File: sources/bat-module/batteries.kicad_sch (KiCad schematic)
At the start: 15 parts, among them J1 53261-0871, J3 67996-110HLF

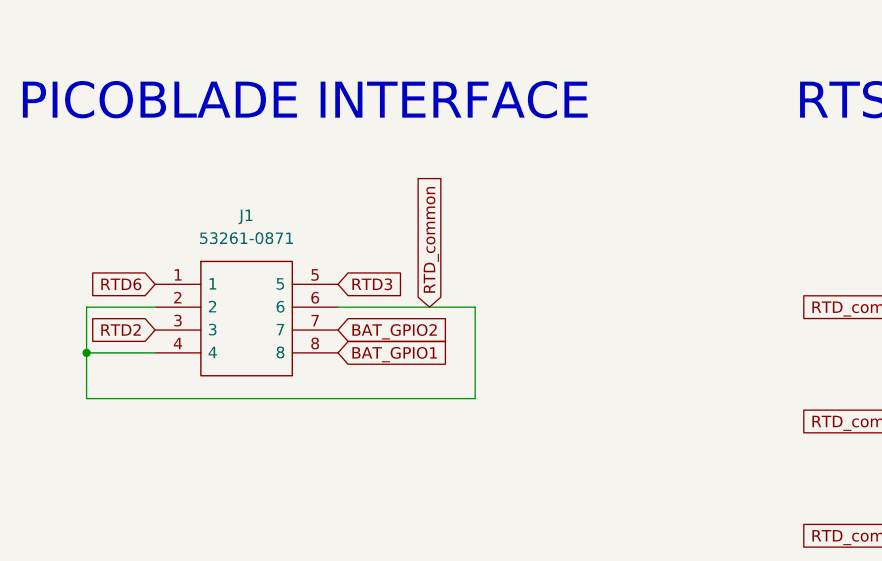
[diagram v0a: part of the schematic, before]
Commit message: i2c-obdh connection and removing picoblade interface #3 #4
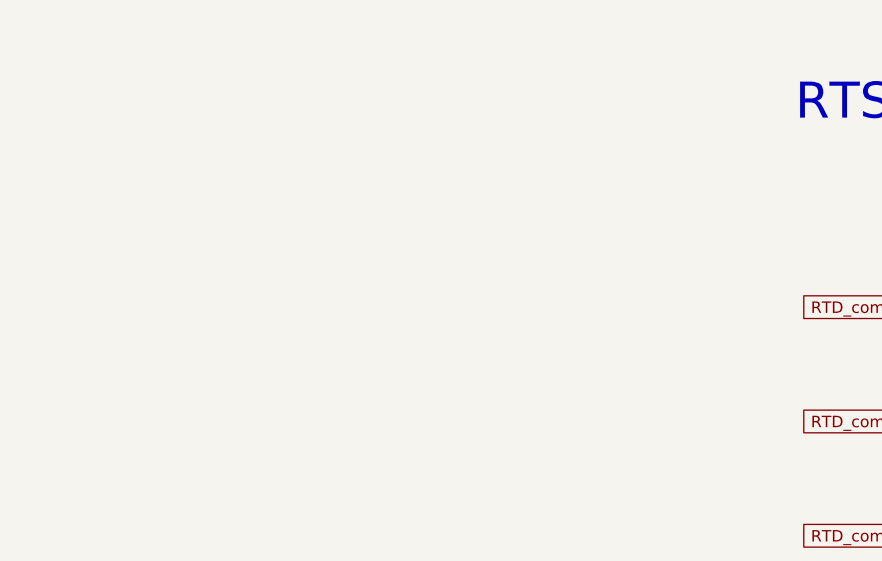
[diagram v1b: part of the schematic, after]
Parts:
- removed J1: 53261-0871, symbol 53261-0871:53261-0871
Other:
- note removed: "PICOBLADE INTERFACE"
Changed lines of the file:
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@@
   (junction (at 241.3 55.88) (diameter 0) (color 0 0 0 0)
   )
-  (junction (at 38.1 68.58) (diameter 0) (color 0 0 0 0)
-  )
   (junction (at 78.74 152.4) (diameter 0) (color 0 0 0 0)
   )
@@
     (stroke (width 0) (type default))
   )
-  (wire (pts (xy 38.1 68.58) (xy 38.1 63.5))
-    (stroke (width 0) (type default))
-  )
   (wire (pts (xy 53.34 160.02) (xy 58.42 160.02))
     (stroke (width 0) (type default))
@@
     (stroke (width 0) (type default))
   )
-  (wire (pts (xy 81.28 63.5) (xy 81.28 73.66))
-    (stroke (width 0) (type default))
-  )
   (wire (pts (xy 210.82 55.88) (xy 215.9 55.88))
     (stroke (width 0) (type default))
@@
     (stroke (width 0) (type default))
   )
-  (wire (pts (xy 81.28 73.66) (xy 38.1 73.66))
-    (stroke (width 0) (type default))
-  )
   (wire (pts (xy 208.28 139.7) (xy 213.36 139.7))
     (stroke (width 0) (type default))
@@
     (stroke (width 0) (type default))
   )
-  (wire (pts (xy 66.04 63.5) (xy 81.28 63.5))
-    (stroke (width 0) (type default))
-  )
   (wire (pts (xy 215.9 76.2) (xy 220.98 76.2))
     (stroke (width 0) (type default))
@@
     (stroke (width 0) (type default))
   )
-  (wire (pts (xy 38.1 63.5) (xy 45.72 63.5))
-    (stroke (width 0) (type default))
-  )
   (wire (pts (xy 45.72 134.62) (xy 58.42 134.62))
     (stroke (width 0) (type default))
@@
     (stroke (width 0) (type default))
   )
-  (wire (pts (xy 45.72 68.58) (xy 38.1 68.58))
-    (stroke (width 0) (type default))
-  )
   (wire (pts (xy 241.3 144.78) (xy 241.3 142.24))
     (stroke (width 0) (type default))
@@
     (stroke (width 0) (type default))
   )
-  (wire (pts (xy 38.1 68.58) (xy 38.1 73.66))
-    (stroke (width 0) (type default))
-  )
   (wire (pts (xy 208.28 147.32) (xy 213.36 147.32))
     (stroke (width 0) (type default))
-  )
-  (text "PICOBLADE INTERFACE" (at 30.48 43.18 0)
-    (effects (font (face "KiCad Font") (size 4 4)) (justify left bottom))
   )
   (text "BATTERIES BOARD TO BOARD \nCONNECTOR TO EPS\n" (at 187.96 124.46 0)
@@
     (effects (font (face "KiCad Font") (size 4 4)) (justify left bottom))
   )
-  (global_label "RTD3" (shape input) (at 66.04 60.96 0) (fields_autoplaced)
-    (effects (font (size 1.27 1.27)) (justify left))
-    (property "Intersheetrefs" "${INTERSHEET_REFS}" (at 73.7423 60.96 0)
-      (effects (font (size 1.27 1.27)) (justify left) hide)
-    )
-  )
   (global_label "VBus" (shape input) (at 243.84 76.2 0) (fields_autoplaced)
     (effects (font (size 1.27 1.27)) (justify left))
@@
     )
   )
-  (global_label "RTD_common" (shape input) (at 76.2 63.5 90) (fields_autoplaced)
-    (effects (font (size 1.27 1.27)) (justify left))
-    (property "Intersheetrefs" "${INTERSHEET_REFS}" (at 76.2 48.1174 90)
-      (effects (font (size 1.27 1.27)) (justify left) hide)
-    )
-  )
   (global_label "-Heater1_Voltage" (shape input) (at 210.82 50.8 180) (fields_autoplaced)
     (effects (font (size 1.27 1.27)) (justify right))
@@
     )
   )
-  (global_label "BAT_GPIO2" (shape input) (at 66.04 66.04 0) (fields_autoplaced)
-    (effects (font (size 1.27 1.27)) (justify left))
-    (property "Intersheetrefs" "${INTERSHEET_REFS}" (at 79.0038 66.04 0)
-      (effects (font (size 1.27 1.27)) (justify left) hide)
-    )
-  )
   (global_label "-VBat" (shape input) (at 53.34 147.32 180) (fields_autoplaced)
     (effects (font (size 1.27 1.27)) (justify right))
@@
     )
   )
-  (global_label "RTD2" (shape input) (at 45.72 66.04 180) (fields_autoplaced)
-    (effects (font (size 1.27 1.27)) (justify right))
-    (property "Intersheetrefs" "${INTERSHEET_REFS}" (at 38.0177 66.04 0)
-      (effects (font (size 1.27 1.27)) (justify right) hide)
-    )
-  )
   (global_label "-VBat" (shape input) (at 203.2 142.24 180) (fields_autoplaced)
     (effects (font (size 1.27 1.27)) (justify right))
@@
     )
   )
-  (global_label "BAT_GPIO1" (shape input) (at 66.04 68.58 0) (fields_autoplaced)
-    (effects (font (size 1.27 1.27)) (justify left))
-    (property "Intersheetrefs" "${INTERSHEET_REFS}" (at 79.0038 68.58 0)
-      (effects (font (size 1.27 1.27)) (justify left) hide)
-    )
-  )
   (global_label "RTD_common" (shape input) (at 132.08 88.9 180) (fields_autoplaced)
     (effects (font (size 1.27 1.27)) (justify right))
@@
     (property "Intersheetrefs" "${INTERSHEET_REFS}" (at 266.2984 50.8 0)
       (effects (font (size 1.27 1.27)) (justify left) hide)
-    )
-  )
-  (global_label "RTD6" (shape input) (at 45.72 60.96 180) (fields_autoplaced)
-    (effects (font (size 1.27 1.27)) (justify right))
-    (property "Intersheetrefs" "${INTERSHEET_REFS}" (at 38.0177 60.96 0)
-      (effects (font (size 1.27 1.27)) (justify right) hide)
     )
   )
@@
         )
       )
-    )
-  )
-  (symbol (lib_id "53261-0871:53261-0871") (at 45.72 60.96 0) (unit 1)
-    (in_bom yes) (on_board yes) (dnp no) (fields_autoplaced)
-    (property "Reference" "J1" (at 55.88 53.34 0)
-      (effects (font (size 1.27 1.27)))
-    )
-    (property "Value" "53261-0871" (at 55.88 55.88 0)
-      (effects (font (size 1.27 1.27)))
-    )
-    (property "Footprint" "" (at 62.23 58.42 0)
-      (effects (font (size 1.27 1.27)) (justify left) hide)
-    )
-    (property "Datasheet" "http://www.molex.com/webdocs/datasheets/pdf/en-us/0532610871_PCB_HEADERS.pdf" (at 62.23 60.96 0)
-      (effects (font (size 1.27 1.27)) (justify left) hide)
-    )
-    (property "Description" "Molex PICOBLADE Series, Series Number 53261, 1.25mm Pitch, 8 Way 1 Row Shrouded Right Angle PCB Header, Surface Mount" (at 62.23 63.5 0)
-      (effects (font (size 1.27 1.27)) (justify left) hide)
-    )
-    (property "Height" "" (at 62.23 66.04 0)
-      (effects (font (size 1.27 1.27)) (justify left) hide)
-    )
-    (property "Mouser Part Number" "538-53261-0871" (at 62.23 68.58 0)
-      (effects (font (size 1.27 1.27)) (justify left) hide)
-    )
-    (property "Mouser Price/Stock" "https://www.mouser.co.uk/ProductDetail/Molex/53261-0871?qs=%252B72YyncTwW%252BggfdCJ7Netw%3D%3D" (at 62.23 71.12 0)
-      (effects (font (size 1.27 1.27)) (justify left) hide)
-    )
-    (property "Manufacturer_Name" "Molex" (at 62.23 73.66 0)
-      (effects (font (size 1.27 1.27)) (justify left) hide)
-    )
-    (property "Manufacturer_Part_Number" "53261-0871" (at 62.23 76.2 0)
-      (effects (font (size 1.27 1.27)) (justify left) hide)
-    )
-    (pin "1")
-    (pin "2")
-    (pin "3")
-    (pin "4")
-    (pin "5")
-    (pin "6")
-    (pin "7")
-    (pin "8")
-    (instances
-      (project "bat-module"
-        (path "/95270ebd-bf33-49a5-840f-dadc8a9f9793/9d70911d-d84d-4b26-a042-f78f6f336ed4"
-          (reference "J1") (unit 1)
-        )
-      )
